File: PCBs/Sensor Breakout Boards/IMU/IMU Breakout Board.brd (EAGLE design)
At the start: 25.4 x 25.4 mm, 5 parts, among them J1 2X6 FEMALE, U1 ICM_20649

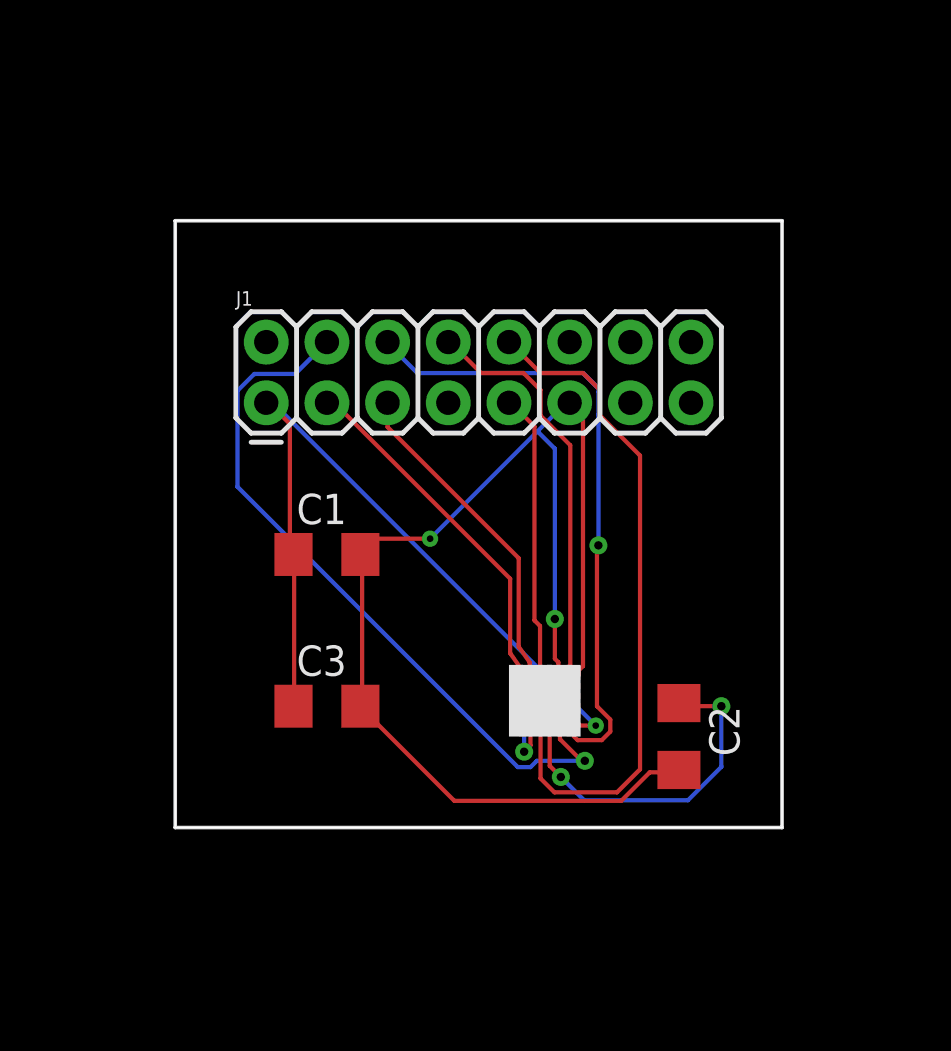
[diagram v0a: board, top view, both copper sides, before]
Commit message: Reshuffled decoupling capacitors on IMU board
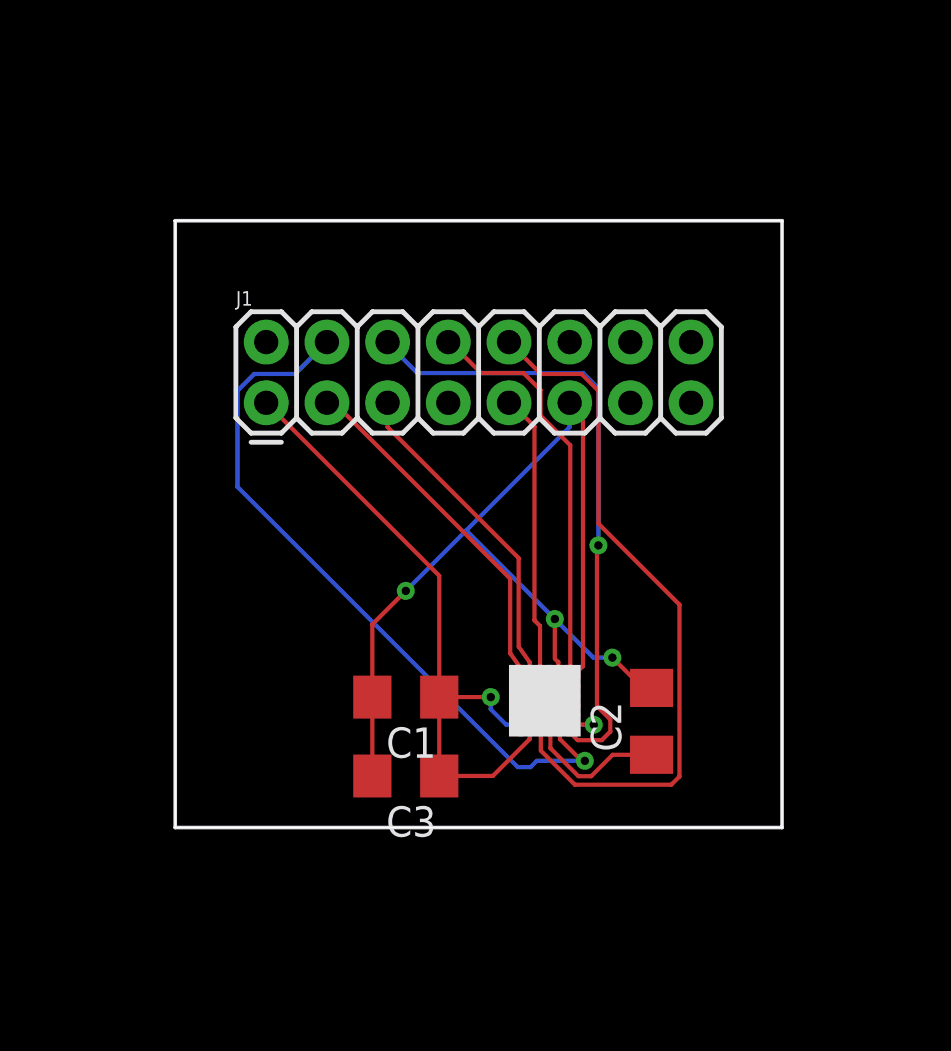
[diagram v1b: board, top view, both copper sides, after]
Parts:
- moved C1 6.82 mm to (9.65, 5.46), turned to 180 degrees
- moved C3 4.41 mm to (9.65, 2.16), turned to 180 degrees
- moved C2 1.31 mm to (19.9, 4.45), turned to 90 degrees
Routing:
- net N$11: track 55.5 -> 43.5 mm, vias 2 -> 3
- net N$9: track 14.1 -> 5.74 mm, vias 2 -> 0
- net N$8: track 37.7 -> 31.3 mm
- net N$7: track 27.9 -> 29.4 mm

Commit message: Added ground planes
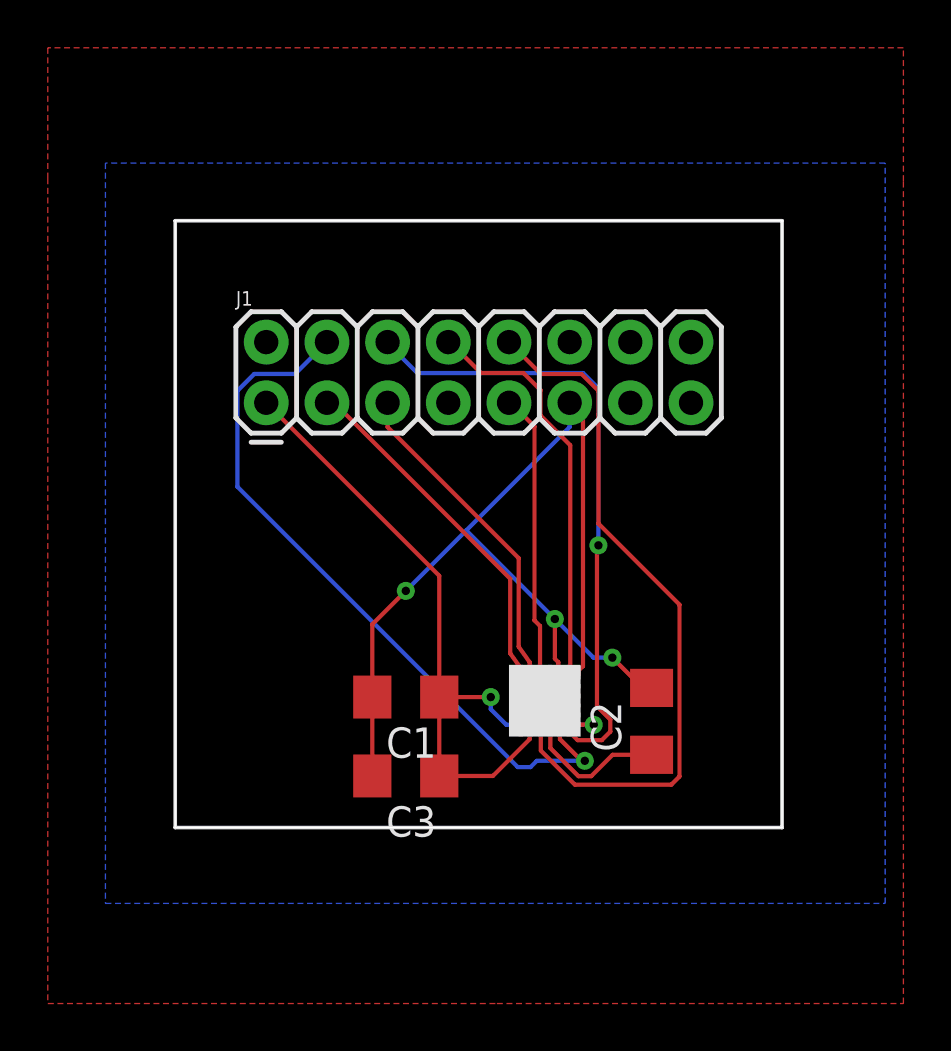
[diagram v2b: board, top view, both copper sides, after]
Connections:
- net N$11 renamed GND
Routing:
- added copper zone on layer 1, net GND
- added copper zone on layer 16, net GND
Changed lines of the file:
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@@
 <wire x1="15.7033" y1="3.32366875" x2="16.87786875" y2="2.1491" width="0.1778" layer="1"/>
-</signal>
-<signal name="N$11">
-<contactref element="U1" pad="P23"/>
-<contactref element="U1" pad="P7"/>
-<contactref element="C2" pad="2"/>
-<contactref element="C3" pad="2"/>
-<contactref element="C1" pad="2"/>
-<contactref element="J1" pad="11"/>
-<wire x1="16.891" y1="6.5786" x2="16.891" y2="6.4008" width="0.1778" layer="1"/>
-<wire x1="17.0688" y1="6.7564" x2="16.891" y2="6.5786" width="0.1778" layer="1"/>
-<wire x1="17.0688" y1="17.2466" x2="17.0688" y2="6.7564" width="0.1778" layer="1"/>
-<wire x1="16.5354" y1="17.78" x2="17.0688" y2="17.2466" width="0.1778" layer="1"/>
-<wire x1="16.891" y1="6.4008" x2="16.82" y2="6.31" width="0.1778" layer="1"/>
-<wire x1="16.5354" y1="17.78" x2="16.51" y2="17.78" width="0.1778" layer="1"/>
-<wire x1="8.252" y1="5.461" x2="8.252" y2="8.506" width="0.1778" layer="1"/>
-<wire x1="8.252" y1="8.506" x2="9.652" y2="9.906" width="0.1778" layer="1"/>
-<via x="9.652" y="9.906" extent="1-16" drill="0.35"/>
-<wire x1="9.652" y1="9.906" x2="12.192" y2="12.446" width="0.1778" layer="16"/>
-<wire x1="12.192" y1="12.446" x2="16.51" y2="16.764" width="0.1778" layer="16"/>
-<wire x1="16.51" y1="16.764" x2="16.51" y2="17.78" width="0.1778" layer="16"/>
-<wire x1="8.252" y1="5.461" x2="8.252" y2="2.159" width="0.1778" layer="1"/>
-<via x="15.8905" y="8.72953125" extent="1-16" drill="0.35"/>
-<wire x1="16.07" y1="6.66" x2="16.0367" y2="6.6933" width="0.1778" layer="1"/>
-<wire x1="16.0367" y1="6.6933" x2="16.0367" y2="6.92046875" width="0.1778" layer="1"/>
-<wire x1="16.0367" y1="6.92046875" x2="15.8905" y2="7.06666875" width="0.1778" layer="1"/>
-<wire x1="15.8905" y1="7.06666875" x2="15.8905" y2="8.72953125" width="0.1778" layer="1"/>
-<wire x1="15.8905" y1="8.72953125" x2="12.192" y2="12.42803125" width="0.1778" layer="16"/>
-<wire x1="12.192" y1="12.42803125" x2="12.192" y2="12.446" width="0.1778" layer="16"/>
-<wire x1="19.939" y1="5.845" x2="19.5649" y2="5.845" width="0.1778" layer="1"/>
-<wire x1="19.5649" y1="5.845" x2="18.2979" y2="7.112" width="0.1778" layer="1"/>
-<via x="18.2979" y="7.112" extent="1-16" drill="0.35"/>
-<wire x1="18.2979" y1="7.112" x2="17.50803125" y2="7.112" width="0.1778" layer="16"/>
-<wire x1="17.50803125" y1="7.112" x2="15.8905" y2="8.72953125" width="0.1778" layer="16"/>
 </signal>
 <signal name="N$5">
@@
 <wire x1="21.1057" y1="2.13453125" x2="21.1057" y2="9.33103125" width="0.1778" layer="1"/>
 </signal>
+<signal name="GND">
+<polygon width="0.1524" layer="1">
+<vertex x="-5.334" y="27.178"/>
+<vertex x="-5.334" y="-7.366"/>
+<vertex x="13.462" y="-7.366"/>
+<vertex x="30.48" y="-7.366"/>
+<vertex x="30.48" y="27.051"/>
+<vertex x="30.48" y="32.639"/>
+<vertex x="21.717" y="32.639"/>
+<vertex x="-5.334" y="32.639"/>
+</polygon>
+<contactref element="U1" pad="P23"/>
+<contactref element="U1" pad="P7"/>
+<contactref element="C2" pad="2"/>
+<contactref element="C3" pad="2"/>
+<contactref element="C1" pad="2"/>
+<contactref element="J1" pad="11"/>
+<wire x1="16.891" y1="6.5786" x2="16.891" y2="6.4008" width="0.1778" layer="1"/>
+<wire x1="17.0688" y1="6.7564" x2="16.891" y2="6.5786" width="0.1778" layer="1"/>
+<wire x1="17.0688" y1="17.2466" x2="17.0688" y2="6.7564" width="0.1778" layer="1"/>
+<wire x1="16.5354" y1="17.78" x2="17.0688" y2="17.2466" width="0.1778" layer="1"/>
+<wire x1="16.891" y1="6.4008" x2="16.82" y2="6.31" width="0.1778" layer="1"/>
+<wire x1="16.5354" y1="17.78" x2="16.51" y2="17.78" width="0.1778" layer="1"/>
+<wire x1="8.252" y1="5.461" x2="8.252" y2="8.506" width="0.1778" layer="1"/>
+<wire x1="8.252" y1="8.506" x2="9.652" y2="9.906" width="0.1778" layer="1"/>
+<via x="9.652" y="9.906" extent="1-16" drill="0.35"/>
+<wire x1="9.652" y1="9.906" x2="12.192" y2="12.446" width="0.1778" layer="16"/>
+<wire x1="12.192" y1="12.446" x2="16.51" y2="16.764" width="0.1778" layer="16"/>
+<wire x1="16.51" y1="16.764" x2="16.51" y2="17.78" width="0.1778" layer="16"/>
+<wire x1="8.252" y1="5.461" x2="8.252" y2="2.159" width="0.1778" layer="1"/>
+<via x="15.8905" y="8.72953125" extent="1-16" drill="0.35"/>
+<wire x1="16.07" y1="6.66" x2="16.0367" y2="6.6933" width="0.1778" layer="1"/>
+<wire x1="16.0367" y1="6.6933" x2="16.0367" y2="6.92046875" width="0.1778" layer="1"/>
+<wire x1="16.0367" y1="6.92046875" x2="15.8905" y2="7.06666875" width="0.1778" layer="1"/>
+<wire x1="15.8905" y1="7.06666875" x2="15.8905" y2="8.72953125" width="0.1778" layer="1"/>
+<wire x1="15.8905" y1="8.72953125" x2="12.192" y2="12.42803125" width="0.1778" layer="16"/>
+<wire x1="12.192" y1="12.42803125" x2="12.192" y2="12.446" width="0.1778" layer="16"/>
+<wire x1="19.939" y1="5.845" x2="19.5649" y2="5.845" width="0.1778" layer="1"/>
+<wire x1="19.5649" y1="5.845" x2="18.2979" y2="7.112" width="0.1778" layer="1"/>
+<via x="18.2979" y="7.112" extent="1-16" drill="0.35"/>
+<wire x1="18.2979" y1="7.112" x2="17.50803125" y2="7.112" width="0.1778" layer="16"/>
+<wire x1="17.50803125" y1="7.112" x2="15.8905" y2="8.72953125" width="0.1778" layer="16"/>
+<polygon width="0.1524" layer="16">
+<vertex x="-2.921" y="27.813"/>
+<vertex x="-2.921" y="-3.175"/>
+<vertex x="29.718" y="-3.175"/>
+<vertex x="29.718" y="27.813"/>
+</polygon>
+</signal>
 </signals>
